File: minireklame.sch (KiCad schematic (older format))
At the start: 33 parts, among them IC1 ATXMEGA64A4U-A, P1 CONN_01X02, P10 CONN_01X04, P11 CONN_01X04, P12 CONN_01X04, P13 CONN_01X04, P14 CONN_01X04, P15 CONN_01X04, P16 CONN_01X04, P17 CONN_01X04, P2 CONN_01X02, P2 CONN_01X04, P3 CONN_01X02, P3 CONN_01X04, P4 CONN_01X04, P5 CONN_01X04, P6 CONN_01X04, P7 CONN_01X04, P8 CONN_01X04, P9 CONN_01X04, U1 TLV1117-33CDCYR, U2 SP3483-EN-L, U3 TLC5955

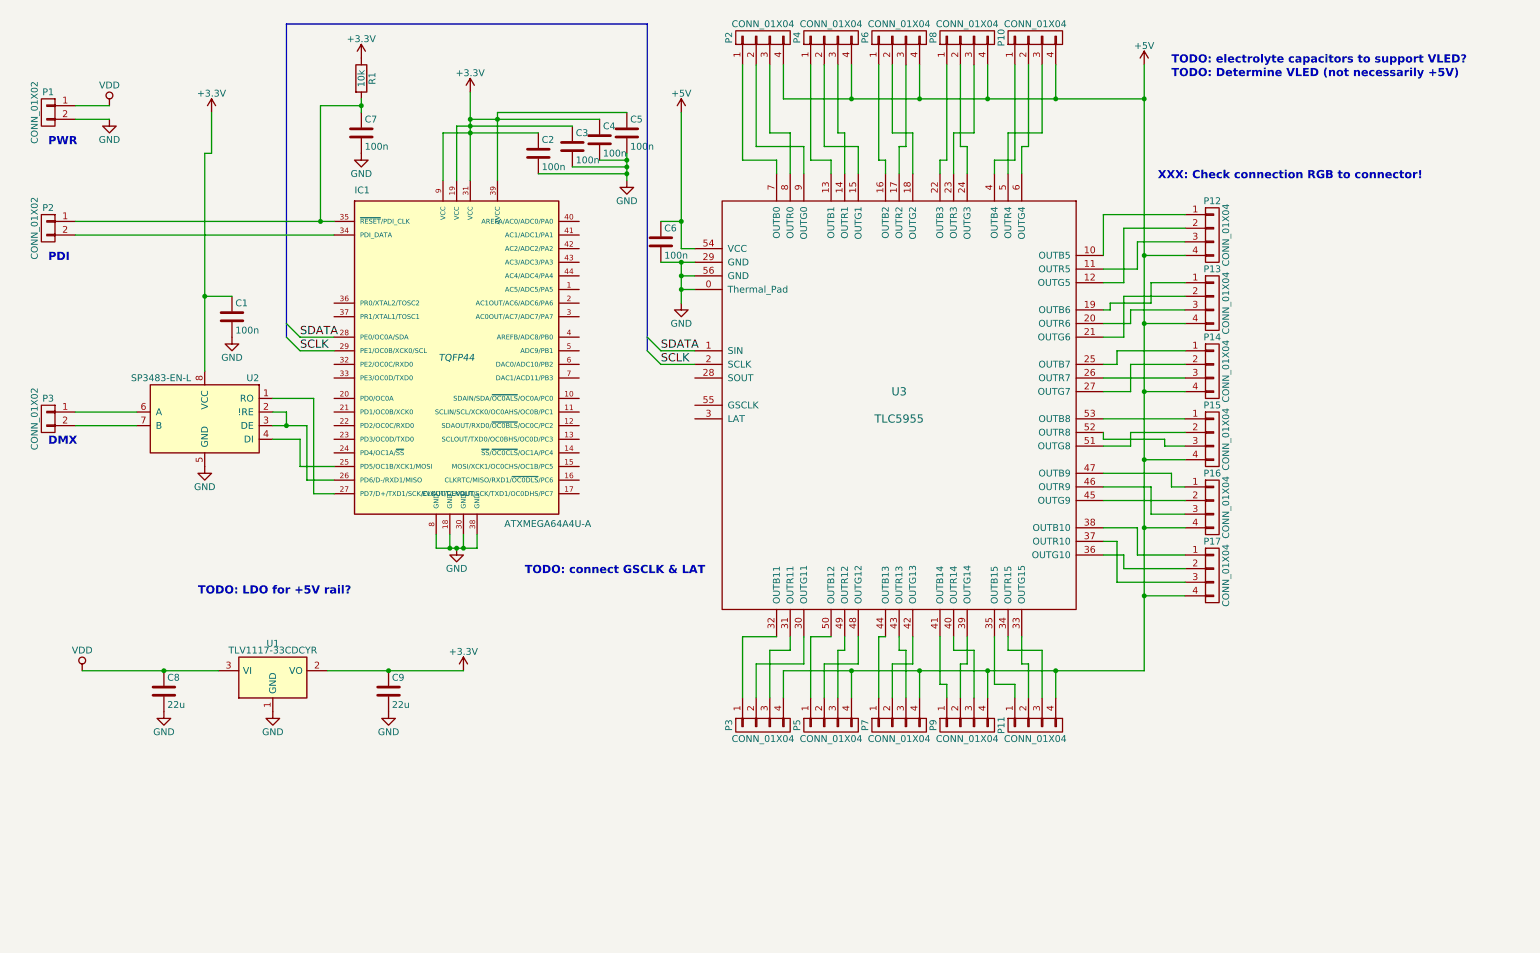
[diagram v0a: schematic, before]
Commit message: place PDI header
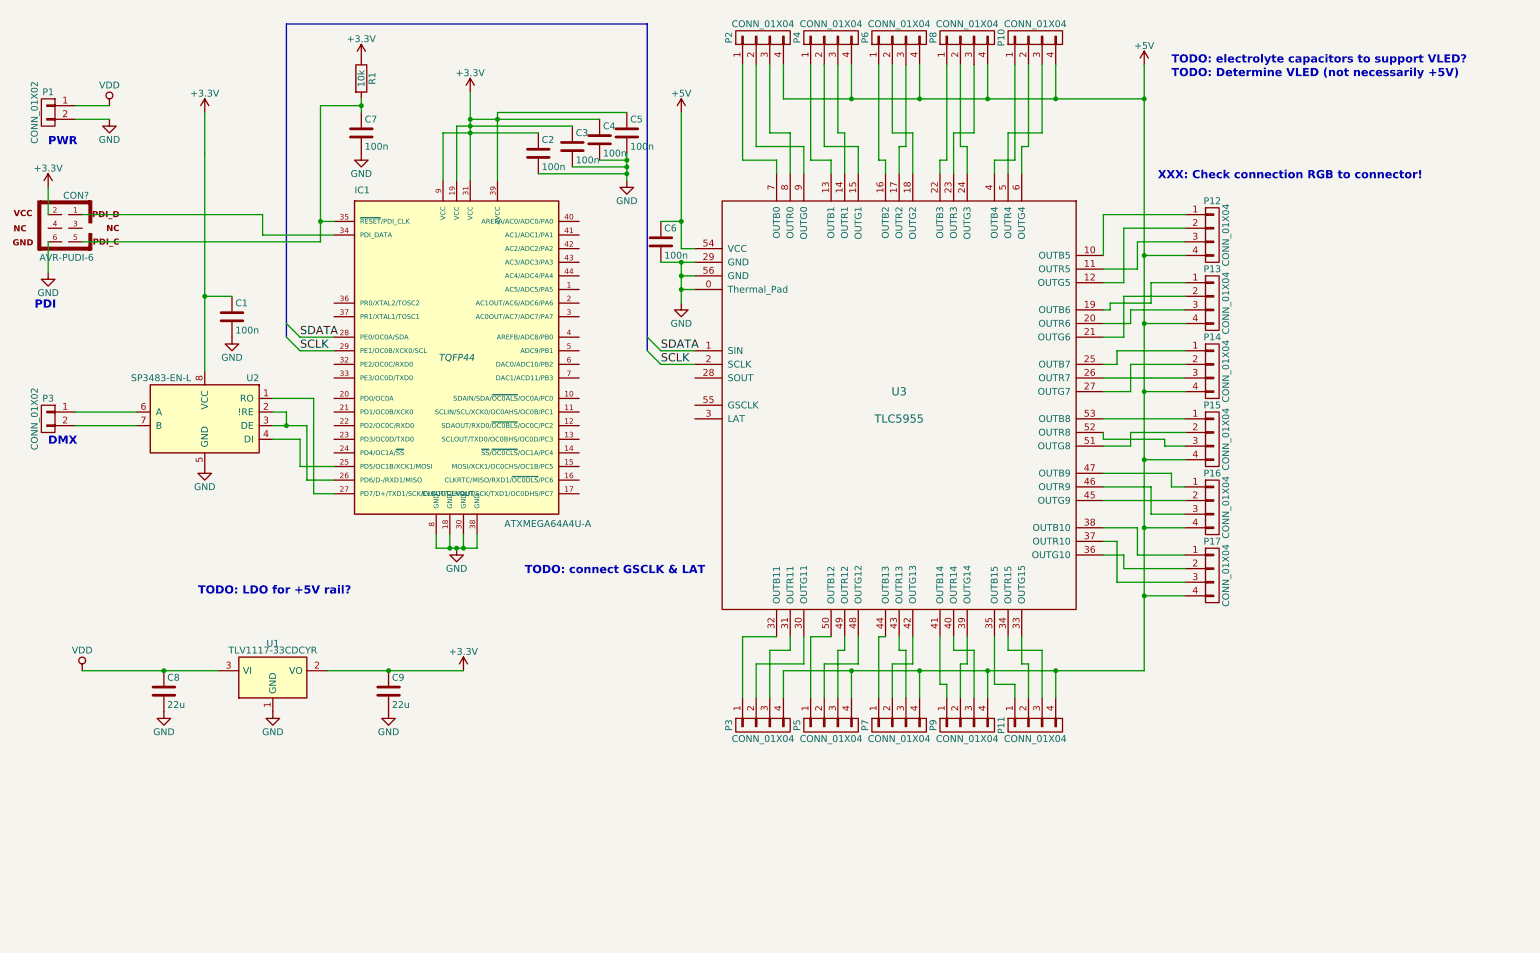
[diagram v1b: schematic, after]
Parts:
- removed P2: CONN_01X02, symbol CONN_01X02
- added CON?: AVR-PUDI-6, AVR-PUDI-6, symbol AVR-PUDI-6
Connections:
- net +3V3: now also CON?.2
- net GND: now also CON?.6
- net at IC1.34 (PDI_DATA): now also CON?.1
- net at C7.1, IC1.35 (~RESET~/PDI_CLK), R1.2: now also CON?.5
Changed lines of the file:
@@
 L +3.3V #PWR02
 U 1 1 58CC36D0
-P 2050 1500
-F 0 "#PWR02" H 2050 1350 50  0001 C CNN
-F 1 "+3.3V" H 2050 1640 50  0000 C CNN
-F 2 "" H 2050 1500 50  0000 C CNN
-F 3 "" H 2050 1500 50  0000 C CNN
-	1    2050 1500
+P 2000 1500
+F 0 "#PWR02" H 2000 1350 50  0001 C CNN
+F 1 "+3.3V" H 2000 1640 50  0000 C CNN
+F 2 "" H 2000 1500 50  0000 C CNN
+F 3 "" H 2000 1500 50  0000 C CNN
+	1    2000 1500
 	1    0    0    -1
 $EndComp
@@
 	1050 3800 1500 3800
 Wire Wire Line
-	2000 1800 2000 3400
+	2000 1800 2000 2850
+Wire Wire Line
+	2000 2850 2000 3400
 Wire Wire Line
 	3700 4600 3700 4700
 Wire Wire Line
-	3700 4700 4000 4700
+	3700 4700 3800 4700
+Wire Wire Line
+	3800 4700 3850 4700
+Wire Wire Line
+	3850 4700 3900 4700
+Wire Wire Line
+	3900 4700 4000 4700
 Wire Wire Line
 	4000 4700 4000 4600
@@
 Connection ~ 3800 4700
 Wire Wire Line
-	5600 2800 5500 2800
-Wire Wire Line
-	5500 2600 5500 2900
+	5500 2800 5600 2800
+Wire Wire Line
+	5500 2600 5500 2700
+Wire Wire Line
+	5500 2700 5500 2800
+Wire Wire Line
+	5500 2800 5500 2900
 Wire Wire Line
 	5600 2700 5500 2700
 Connection ~ 5500 2800
 Wire Wire Line
-	5350 2600 5600 2600
+	5350 2600 5500 2600
+Wire Wire Line
+	5500 2600 5600 2600
 Connection ~ 5500 2700
 Wire Wire Line
 	3750 1650 3750 2000
 Wire Wire Line
-	4150 1500 4150 2000
-Wire Wire Line
-	5600 2500 5500 2500
-Wire Wire Line
-	5500 2500 5500 1500
+	4150 1500 4150 1550
+Wire Wire Line
+	4150 1550 4150 2000
+Wire Wire Line
+	5500 2500 5600 2500
+Wire Wire Line
+	5500 1500 5500 2300
+Wire Wire Line
+	5500 2300 5500 2500
 Wire Wire Line
 	5600 3250 5350 3250
@@
 	5600 3350 5350 3350
 Wire Bus Line
-	5250 850  5250 3250
+	5250 850  5250 3150
+Wire Bus Line
+	5250 3150 5250 3250
 Wire Bus Line
 	5250 850  2600 850
 Wire Bus Line
-	2600 850  2600 3150
+	2600 850  2600 3050
+Wire Bus Line
+	2600 3050 2600 3150
 Wire Wire Line
 	2700 3150 2950 3150
@@
 	2700 4100 2950 4100
 Wire Wire Line
-	2500 3800 2750 3800
+	2500 3800 2600 3800
+Wire Wire Line
+	2600 3800 2750 3800
 Wire Wire Line
 	2750 3800 2750 4200
@@
 	2800 4300 2950 4300
 Wire Wire Line
-	2050 1500 2050 1800
-Wire Wire Line
-	2050 1800 2000 1800
+	2000 1500 2000 1800
+Wire Wire Line
+	2000 1800 2000 1800
 Wire Wire Line
 	6250 1150 6250 1400
 Wire Wire Line
-	6250 1400 8900 1400
-Wire Wire Line
-	8900 1150 8900 5600
+	6250 1400 6750 1400
+Wire Wire Line
+	6750 1400 7250 1400
+Wire Wire Line
+	7250 1400 7750 1400
+Wire Wire Line
+	7750 1400 8250 1400
+Wire Wire Line
+	8250 1400 8900 1400
+Wire Wire Line
+	8900 5600 8900 5050
+Wire Wire Line
+	8900 5050 8900 4550
+Wire Wire Line
+	8900 4550 8900 4050
+Wire Wire Line
+	8900 4050 8900 3550
+Wire Wire Line
+	8900 3550 8900 3050
+Wire Wire Line
+	8900 3050 8900 2550
+Wire Wire Line
+	8900 2550 8900 1400
+Wire Wire Line
+	8900 1400 8900 1150
 Wire Wire Line
 	6750 1150 6750 1400
@@
 	6250 5800 6250 5600
 Wire Wire Line
-	6250 5600 8900 5600
+	6250 5600 6750 5600
+Wire Wire Line
+	6750 5600 7250 5600
+Wire Wire Line
+	7250 5600 7750 5600
+Wire Wire Line
+	7750 5600 8250 5600
+Wire Wire Line
+	8250 5600 8900 5600
 Connection ~ 8900 5050
 Wire Wire Line
@@
 	4150 1500 5100 1500
 Wire Wire Line
-	3950 1350 3950 2000
-Wire Wire Line
-	3950 1550 4900 1550
+	3950 1350 3950 1550
+Wire Wire Line
+	3950 1550 3950 1600
+Wire Wire Line
+	3950 1600 3950 1650
+Wire Wire Line
+	3950 1650 3950 2000
+Wire Wire Line
+	3950 1550 4150 1550
+Wire Wire Line
+	4150 1550 4900 1550
 Wire Wire Line
 	3850 2000 3850 1600
 Wire Wire Line
-	3850 1600 4700 1600
-Wire Wire Line
-	3750 1650 4450 1650
+	3850 1600 3950 1600
+Wire Wire Line
+	3950 1600 4700 1600
+Wire Wire Line
+	3750 1650 3950 1650
+Wire Wire Line
+	3950 1650 4450 1650
 Connection ~ 3950 1550
 Connection ~ 3950 1650
@@
 Connection ~ 4150 1550
 Wire Wire Line
-	4450 1950 5100 1950
-Wire Wire Line
-	5100 1800 5100 2000
+	5100 1950 4450 1950
+Wire Wire Line
+	5100 1800 5100 1850
+Wire Wire Line
+	5100 1850 5100 1900
+Wire Wire Line
+	5100 1900 5100 1950
+Wire Wire Line
+	5100 1950 5100 2000
 Wire Wire Line
 	4700 1900 5100 1900
@@
 $EndComp
 Wire Wire Line
-	1100 5600 2100 5600
-Wire Wire Line
-	2900 5600 3900 5600
+	1100 5600 1700 5600
+Wire Wire Line
+	1700 5600 2100 5600
+Wire Wire Line
+	2900 5600 3350 5600
+Wire Wire Line
+	3350 5600 3900 5600
 $Comp
 L GND #PWR012
@@
 $EndComp
 Wire Wire Line
-	1050 2300 2950 2300
-$Comp
-L CONN_01X02 P2
-U 1 1 58DDB060
-P 850 2350
-F 0 "P2" H 850 2500 50  0000 C CNN
-F 1 "CONN_01X02" V 950 2350 50  0000 C CNN
-F 2 "" H 850 2350 50  0000 C CNN
-F 3 "" H 850 2350 50  0000 C CNN
-	1    850  2350
-	-1   0    0    -1
-$EndComp
-Wire Wire Line
 	2850 1450 3150 1450
 Wire Wire Line
-	3150 1400 3150 1500
+	3150 1400 3150 1450
+Wire Wire Line
+	3150 1450 3150 1500
 Connection ~ 3150 1450
 $Comp
@@
 	1050 1550 1300 1550
 Wire Wire Line
-	2850 1450 2850 2300
-Wire Wire Line
-	2950 2400 1050 2400
-Connection ~ 2850 2300
+	2850 2450 2850 2300
+Wire Wire Line
+	2850 2300 2850 1450
 Text Notes 850  1750 0    60   ~ 12
 PWR
-Text Notes 850  2600 0    60   ~ 12
+Text Notes 750  2950 0    60   ~ 12
 PDI
 Text Notes 850  3950 0    60   ~ 12
@@
 Text Notes 4350 4900 0    60   ~ 12
 TODO: connect GSCLK & LAT
+$Comp
+L AVR-PUDI-6 CON?
+U 1 1 5919E95A
+P 975 2350
+F 0 "CON?" H 895 2590 50  0000 C CNN
+F 1 "AVR-PUDI-6" H 765 2105 50  0000 L BNN
+F 2 "AVR-PUDI-6" V 530 2385 50  0001 C CNN
+F 3 "" H 975 2350 50  0001 C CNN
+	1    975  2350
+	-1   0    0    -1
+$EndComp
+Wire Wire Line
+	1100 2450 2850 2450
+Wire Wire Line
+	2950 2300 2850 2300
+Connection ~ 2850 2300
+Wire Wire Line
+	2950 2400 2425 2400
+Wire Wire Line
+	2425 2400 2425 2250
+Wire Wire Line
+	2425 2250 1100 2250
+Wire Wire Line
+	850  2250 850  2050
+Wire Wire Line
+	850  2450 850  2675
+$Comp
+L GND #PWR?
+U 1 1 5919FF5A
+P 850 2675
+F 0 "#PWR?" H 850 2425 50  0001 C CNN
+F 1 "GND" H 850 2525 50  0000 C CNN
+F 2 "" H 850 2675 50  0001 C CNN
+F 3 "" H 850 2675 50  0001 C CNN
+	1    850  2675
+	1    0    0    -1
+$EndComp
+$Comp
+L +3.3V #PWR?
+U 1 1 591A008E
+P 850 2050
+F 0 "#PWR?" H 850 1900 50  0001 C CNN
+F 1 "+3.3V" H 850 2190 50  0000 C CNN
+F 2 "" H 850 2050 50  0000 C CNN
+F 3 "" H 850 2050 50  0000 C CNN
+	1    850  2050
+	1    0    0    -1
+$EndComp
 $EndSCHEMATC

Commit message: tidying up junctions and moving 100n Cs for better readability
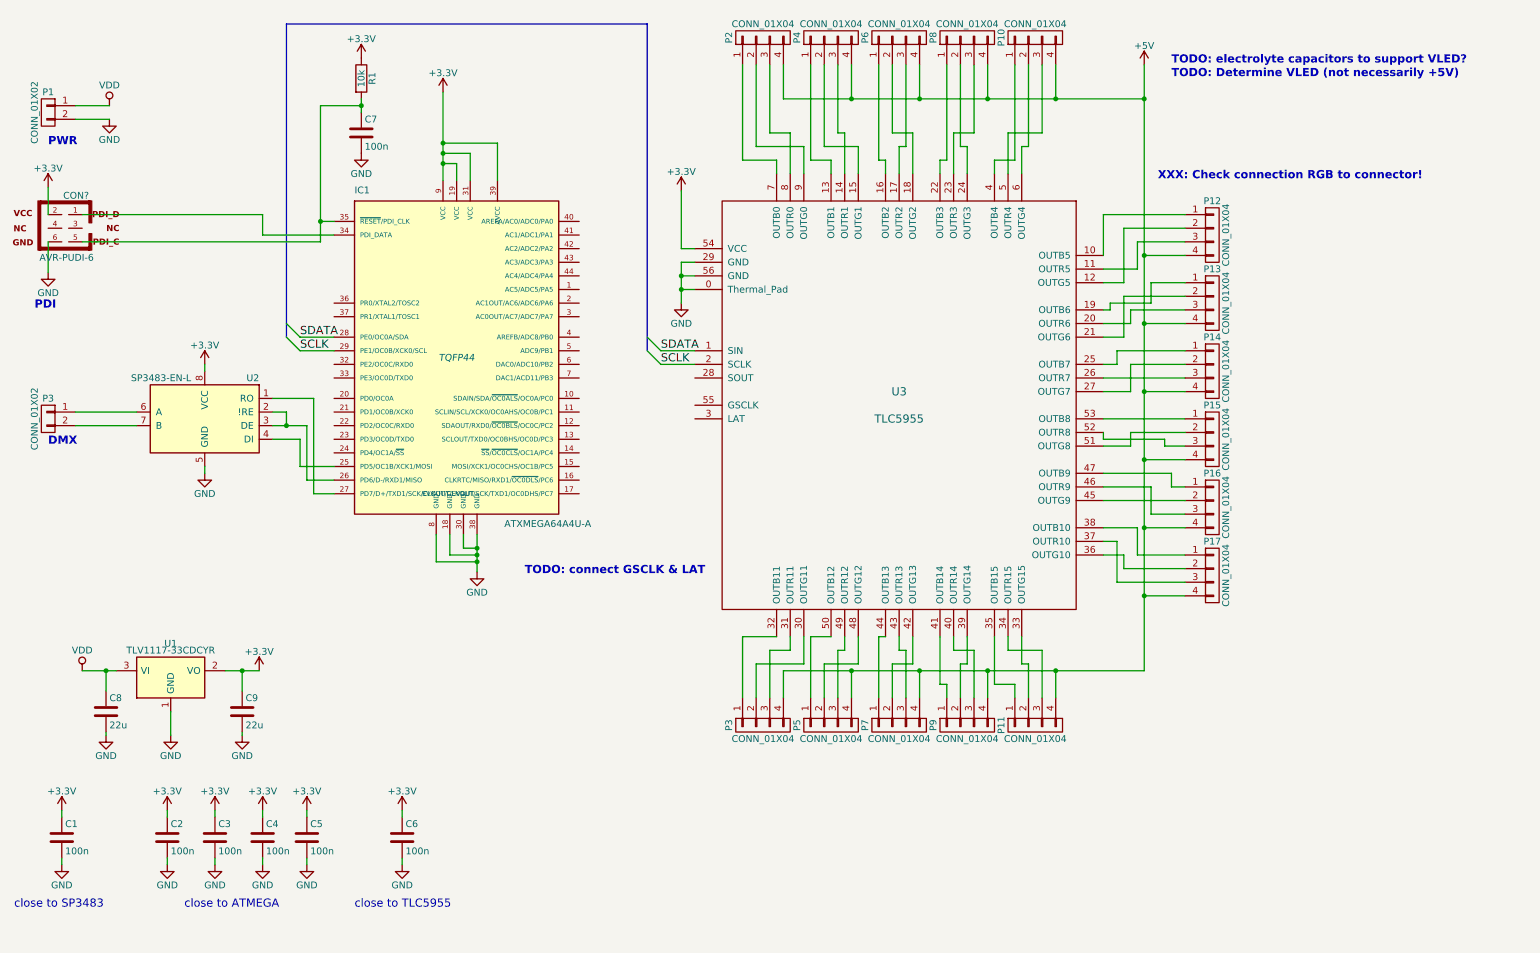
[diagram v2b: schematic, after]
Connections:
- net +3V3: now also C6.1, U3.54 (VCC)
- net +5V: no longer C6.1, U3.54 (VCC)
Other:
- note added: "close to ATMEGA"
- note added: "close to SP3483"
- note added: "close to TLC5955"
- note removed: "TODO: LDO for +5V rail?"
- moved on the sheet: C1, C2, C3, C4, C5, C6, C8, C9, U1
